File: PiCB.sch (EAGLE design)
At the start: 30 parts

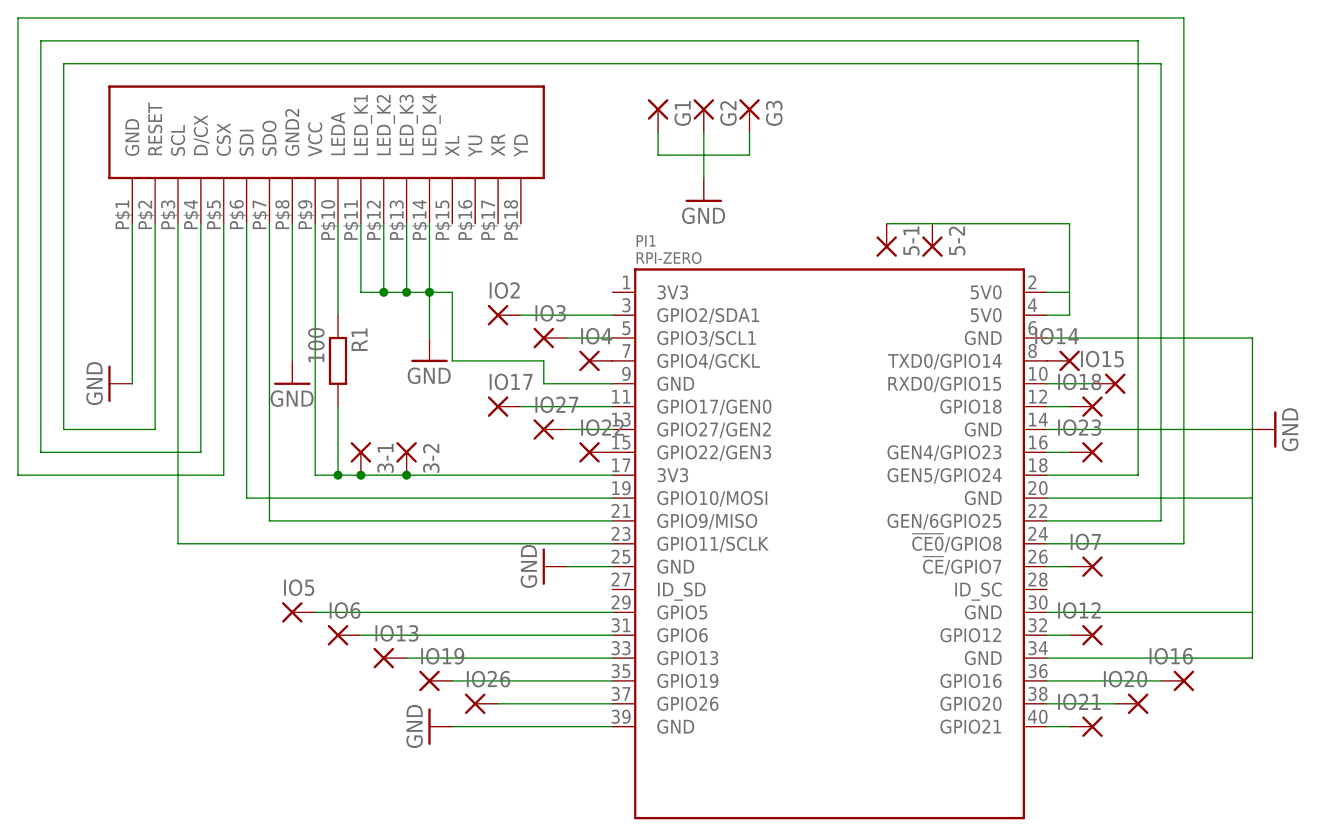
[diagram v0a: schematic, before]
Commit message: Add files via upload
made the gpio on 2 rows, added more grounds and better spacing
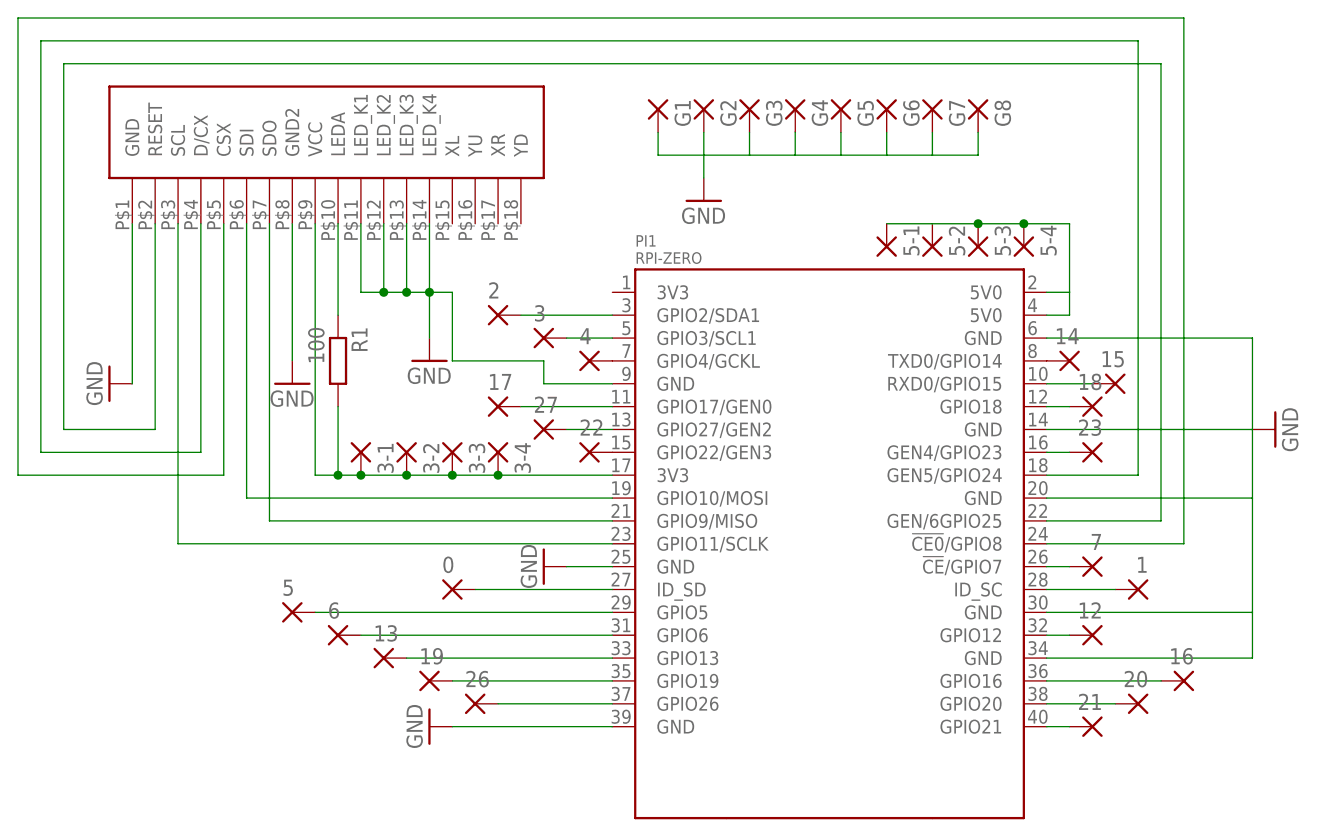
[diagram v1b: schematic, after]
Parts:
- added 0, 1, 3-3, 3-4, 5-3, 5-4, G4, G5, G6, G7, G8: (no value), wirepad:1,6/0,8
- renumbered IO12 to 12, IO13 to 13, IO14 to 14, IO15 to 15, IO16 to 16, IO17 to 17, IO18 to 18, IO19 to 19, IO2 to 2, IO20 to 20, IO21 to 21, IO22 to 22, IO23 to 23, IO26 to 26, IO27 to 27, IO3 to 3, IO4 to 4, IO5 to 5, IO6 to 6, IO7 to 7
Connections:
- new net N$31: 0.P, PI1.ID_SD
- new net N$32: 1.P, PI1.ID_SC
- net 5V0@2: now also 5-3.P, 5-4.P
- net GND: now also G4.P, G5.P, G6.P, G7.P, G8.P
- net N$19: now also 3-3.P, 3-4.P
